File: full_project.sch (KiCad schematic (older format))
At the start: 45 parts, among them J1 Conn_01x16, J10 Screw_Terminal_01x02, J12 V_OFFSET, J14 Conn_01x02, J2 Raspberry_Pi_2_3, J3 Conn_01x08, J4 Screw_Terminal_01x04_titrator, J5 RF_Shield_Two_Pieces, J6 BNC_Jack, J7 SJ-43515TS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

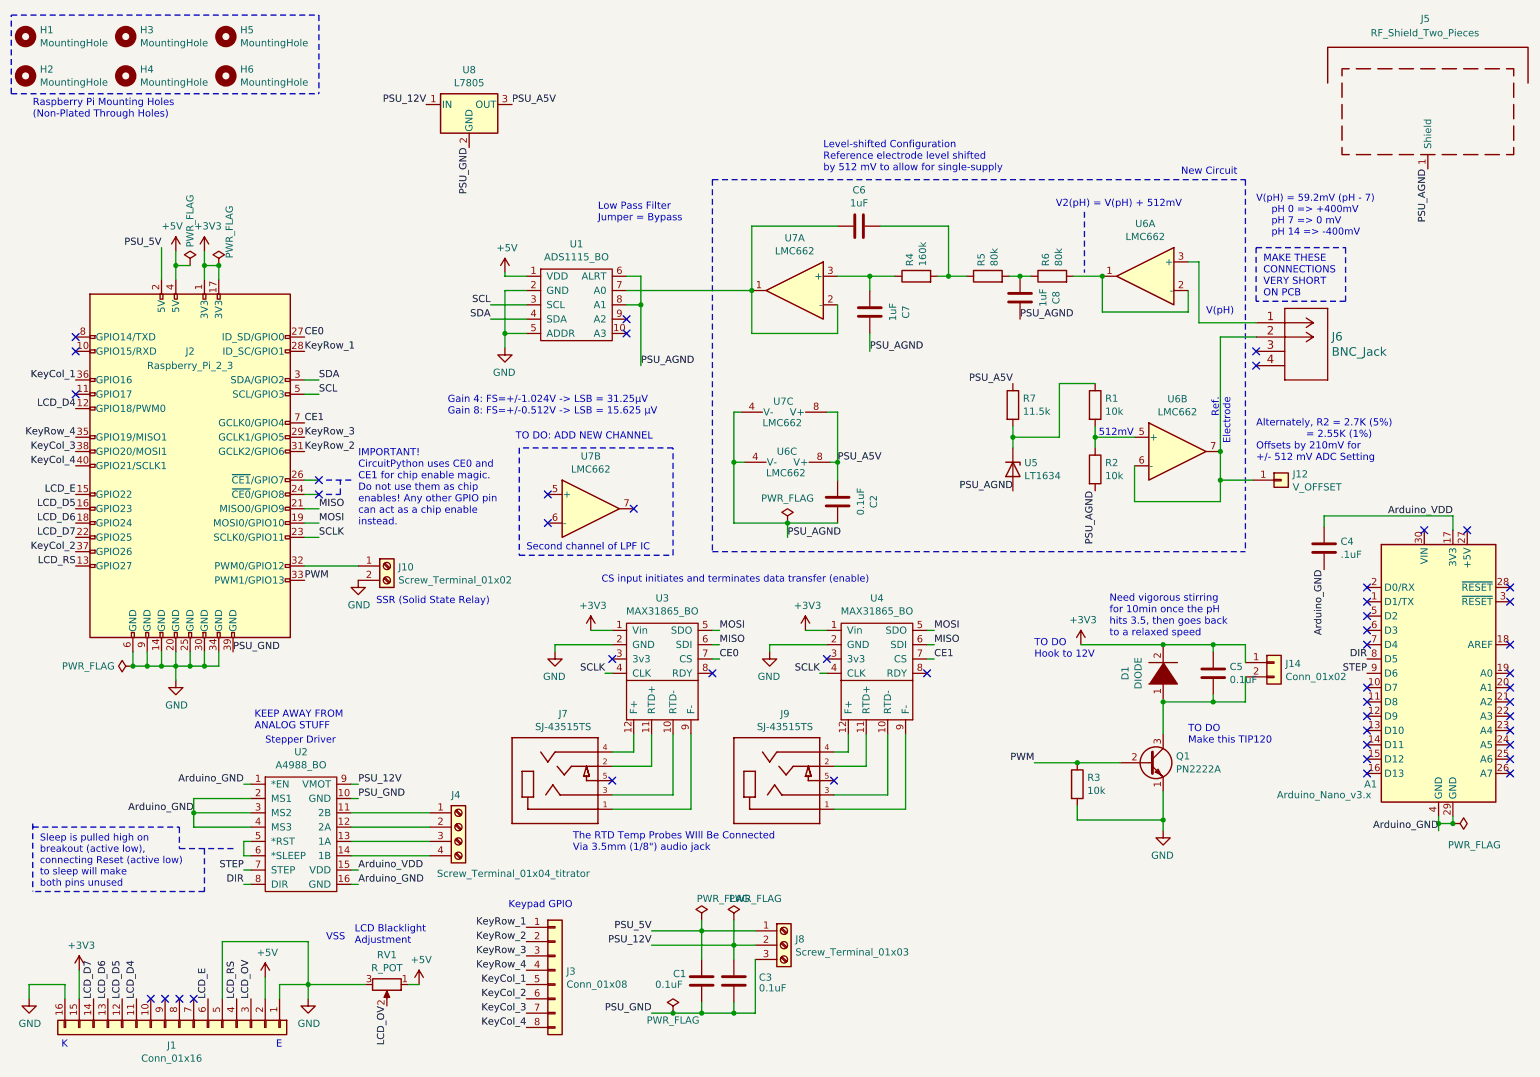
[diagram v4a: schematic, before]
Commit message: Added offset voltage follower for ADC in schematic, added extra notes
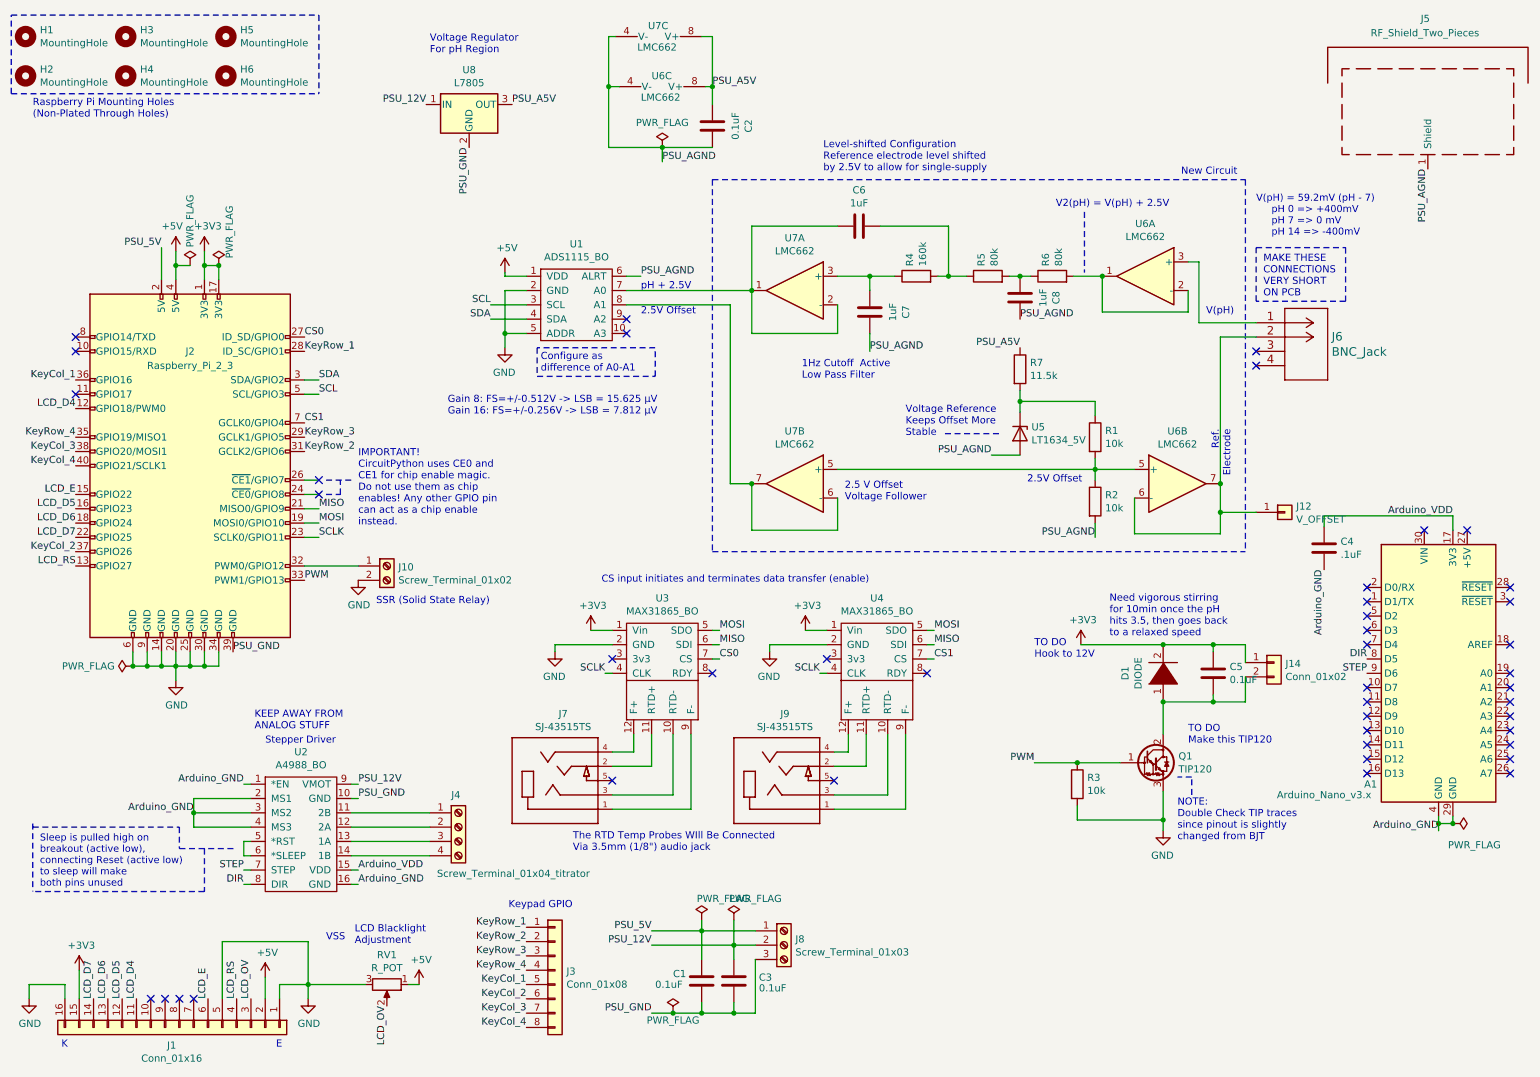
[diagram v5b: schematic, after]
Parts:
- removed Q1: PN2222A, Package_TO_SOT_THT:TO-92_Inline, symbol Transistor_BJT:PN2222A
- added Q1: TIP120, Package_TO_SOT_THT:TO-220-3_Vertical, symbol Transistor_BJT:TIP120
- U5: value LT1634 -> LT1634_5V
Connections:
- net GND: now also Q1.3 (E)
- net PSU_AGND: no longer U1.8 (A1)
- net PWM: now also Q1.1 (B)
- net at C5.2, D1.1 (K), J14.2 (Pin_2): now also Q1.2 (C)
- net at U7.5 (+): now also R1.2, R2.1, U6.5 (+)
- net at U7.6 (-): now also U1.8 (A1), U7.7
- net CE0 renamed CS0
- net CE1 renamed CS1
- no-connect marks 47 -> 44
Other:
- note added: "1Hz Cutoff Active \nLow Pass Filter"
- note added: "2.5 V Offset\nVoltage Follower"
- note added: "2.5V Offset"
- note added: "Configure as \ndifference of A0-A1"
- note added: "Gain 8: FS=+/-0.512V -> LSB = 15.625 μV\nGain 16: FS=+/-0.256V -> LSB = 7.812 μV"
- note added: "Level-shifted Configuration\nReference electrode level shifted \nby 2.5V to allow for single-supply"
- note added: "NOTE:\nDouble Check TIP traces\nsince pinout is slightly\nchanged from BJT"
- note added: "V2(pH) = V(pH) + 2.5V"
- note added: "Voltage Reference\nKeeps Offset More \nStable"
- note added: "Voltage Regulator\nFor pH Region"
- note added: "pH + 2.5V"
- note removed: "512mV"
- note removed: "Alternately, R2 = 2.7K (5%) \n = 2.55K (1%)\nOffsets by 210mV for\n+/- 512 mV ADC Setting"
- note removed: "Gain 4: FS=+/-1.024V -> LSB = 31.25μV\nGain 8: FS=+/-0.512V -> LSB = 15.625 μV"
- note removed: "Level-shifted Configuration\nReference electrode level shifted \nby 512 mV to allow for single-supply"
- note removed: "Low Pass Filter\nJumper = Bypass"
- note removed: "Second channel of LPF IC"
- note removed: "TO DO: ADD NEW CHANNEL"
- note removed: "V2(pH) = V(pH) + 512mV"
- moved on the sheet: C2, J12, R1, R2, R7, U5, U6B, U6C, U7B, U7C
